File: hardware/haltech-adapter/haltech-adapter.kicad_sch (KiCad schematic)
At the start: 4 parts, among them J1 6437288-1, J2 Conn_02x32_Odd_Even

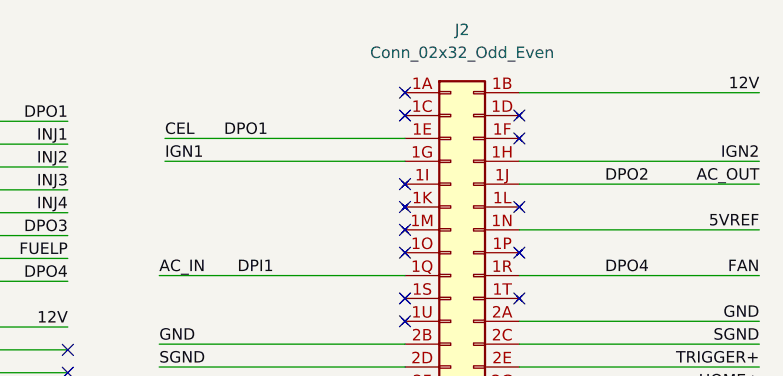
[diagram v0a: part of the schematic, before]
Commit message: Finish Haltech adapter
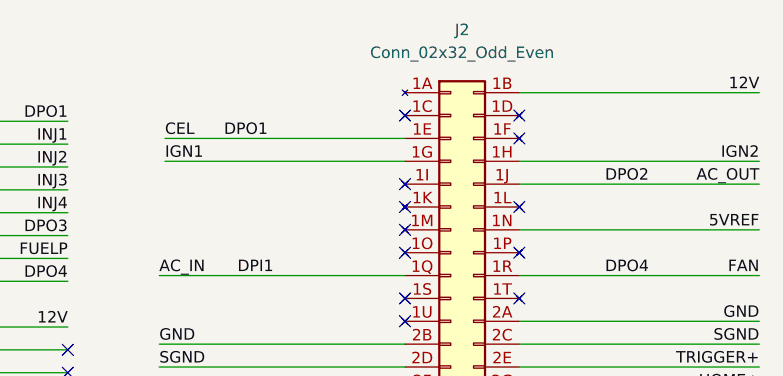
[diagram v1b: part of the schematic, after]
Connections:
- no-connect marks 44 -> 43
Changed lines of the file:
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@@
   (no_connect (at 19.685 48.895))
   (no_connect (at 116.84 38.1))
-  (no_connect (at 116.84 27.94))
   (no_connect (at 129.54 96.52))
   (no_connect (at 116.84 83.82))
